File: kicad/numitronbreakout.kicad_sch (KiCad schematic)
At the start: 8 parts, among them J1 Conn_01x06, U1 HV5812WG-G, U2 IV-12, U3 IV-12, U4 LM317_TO-220

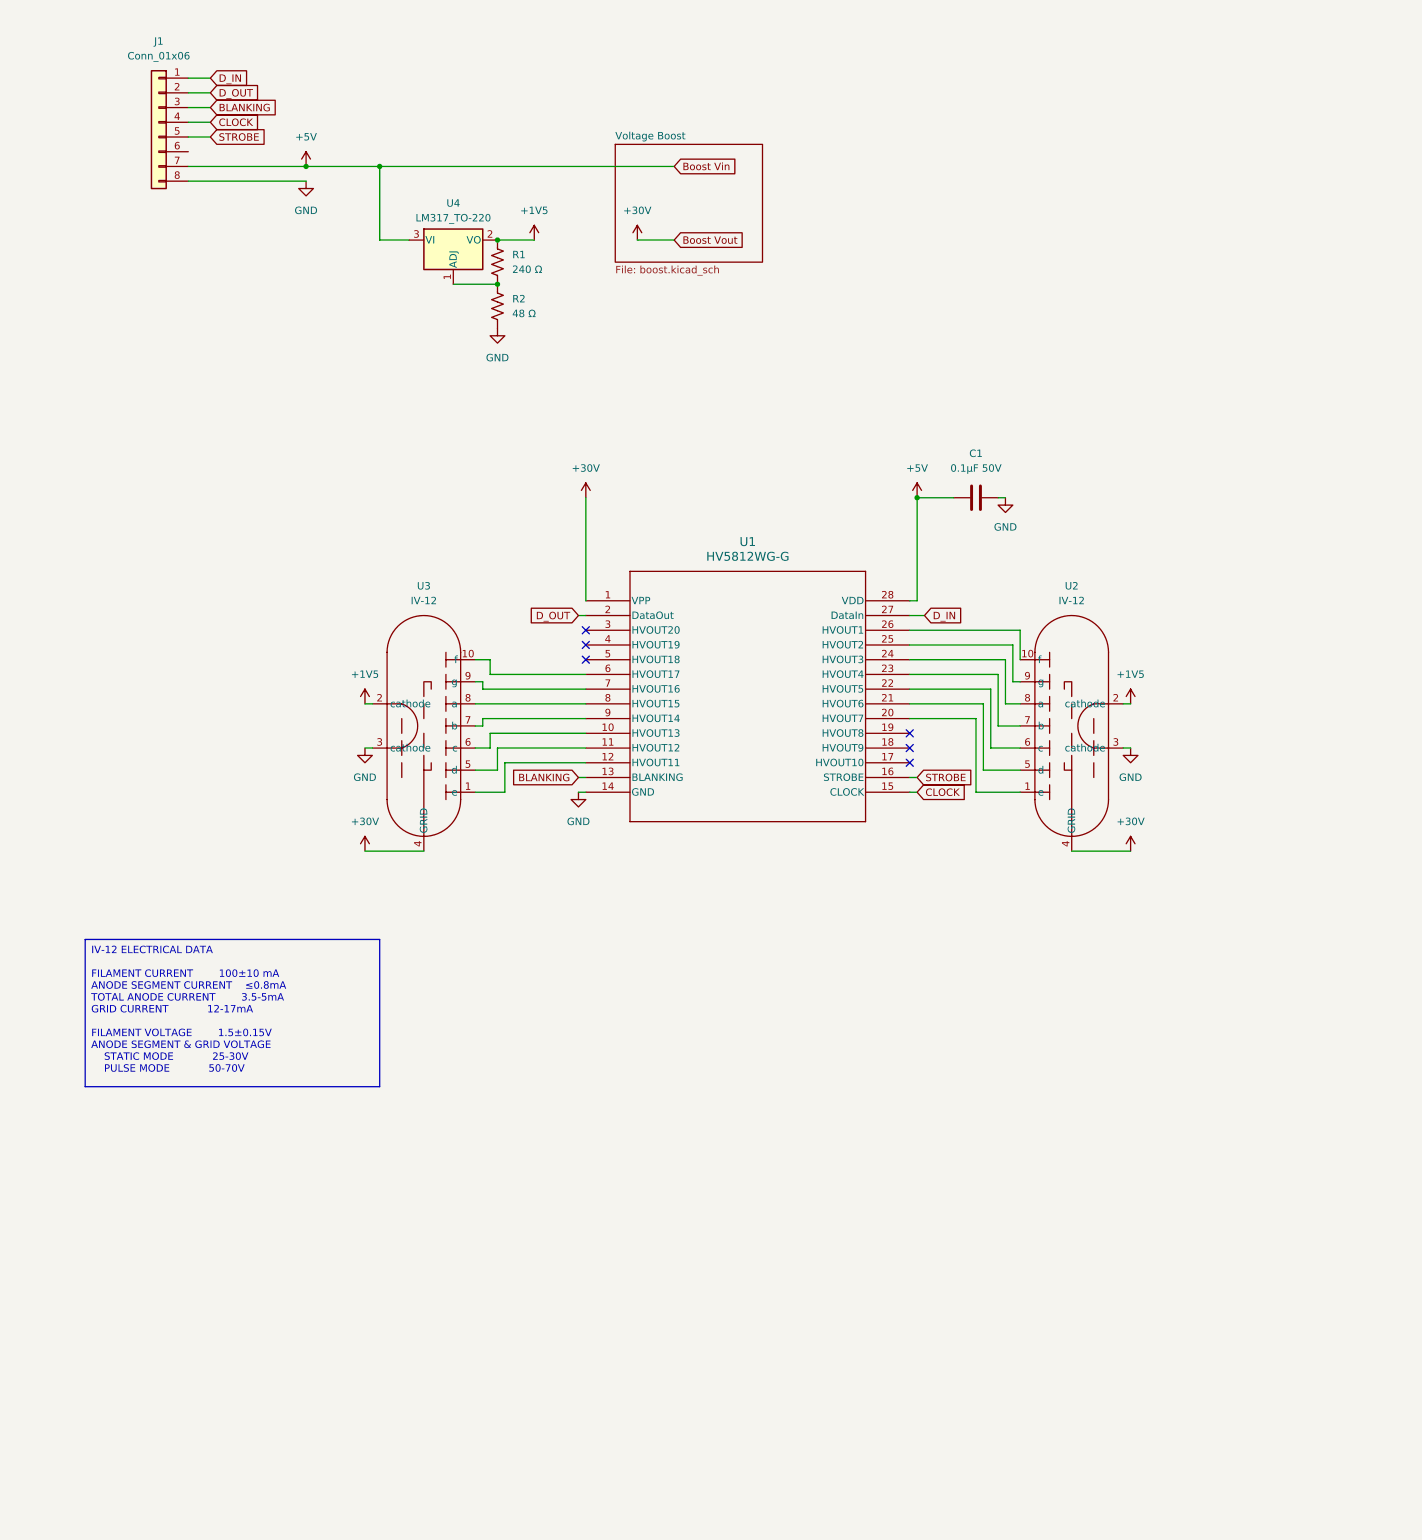
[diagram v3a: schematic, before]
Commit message: boost converter refactor
new design from web bench to reduce bom complexity & increase efficiency
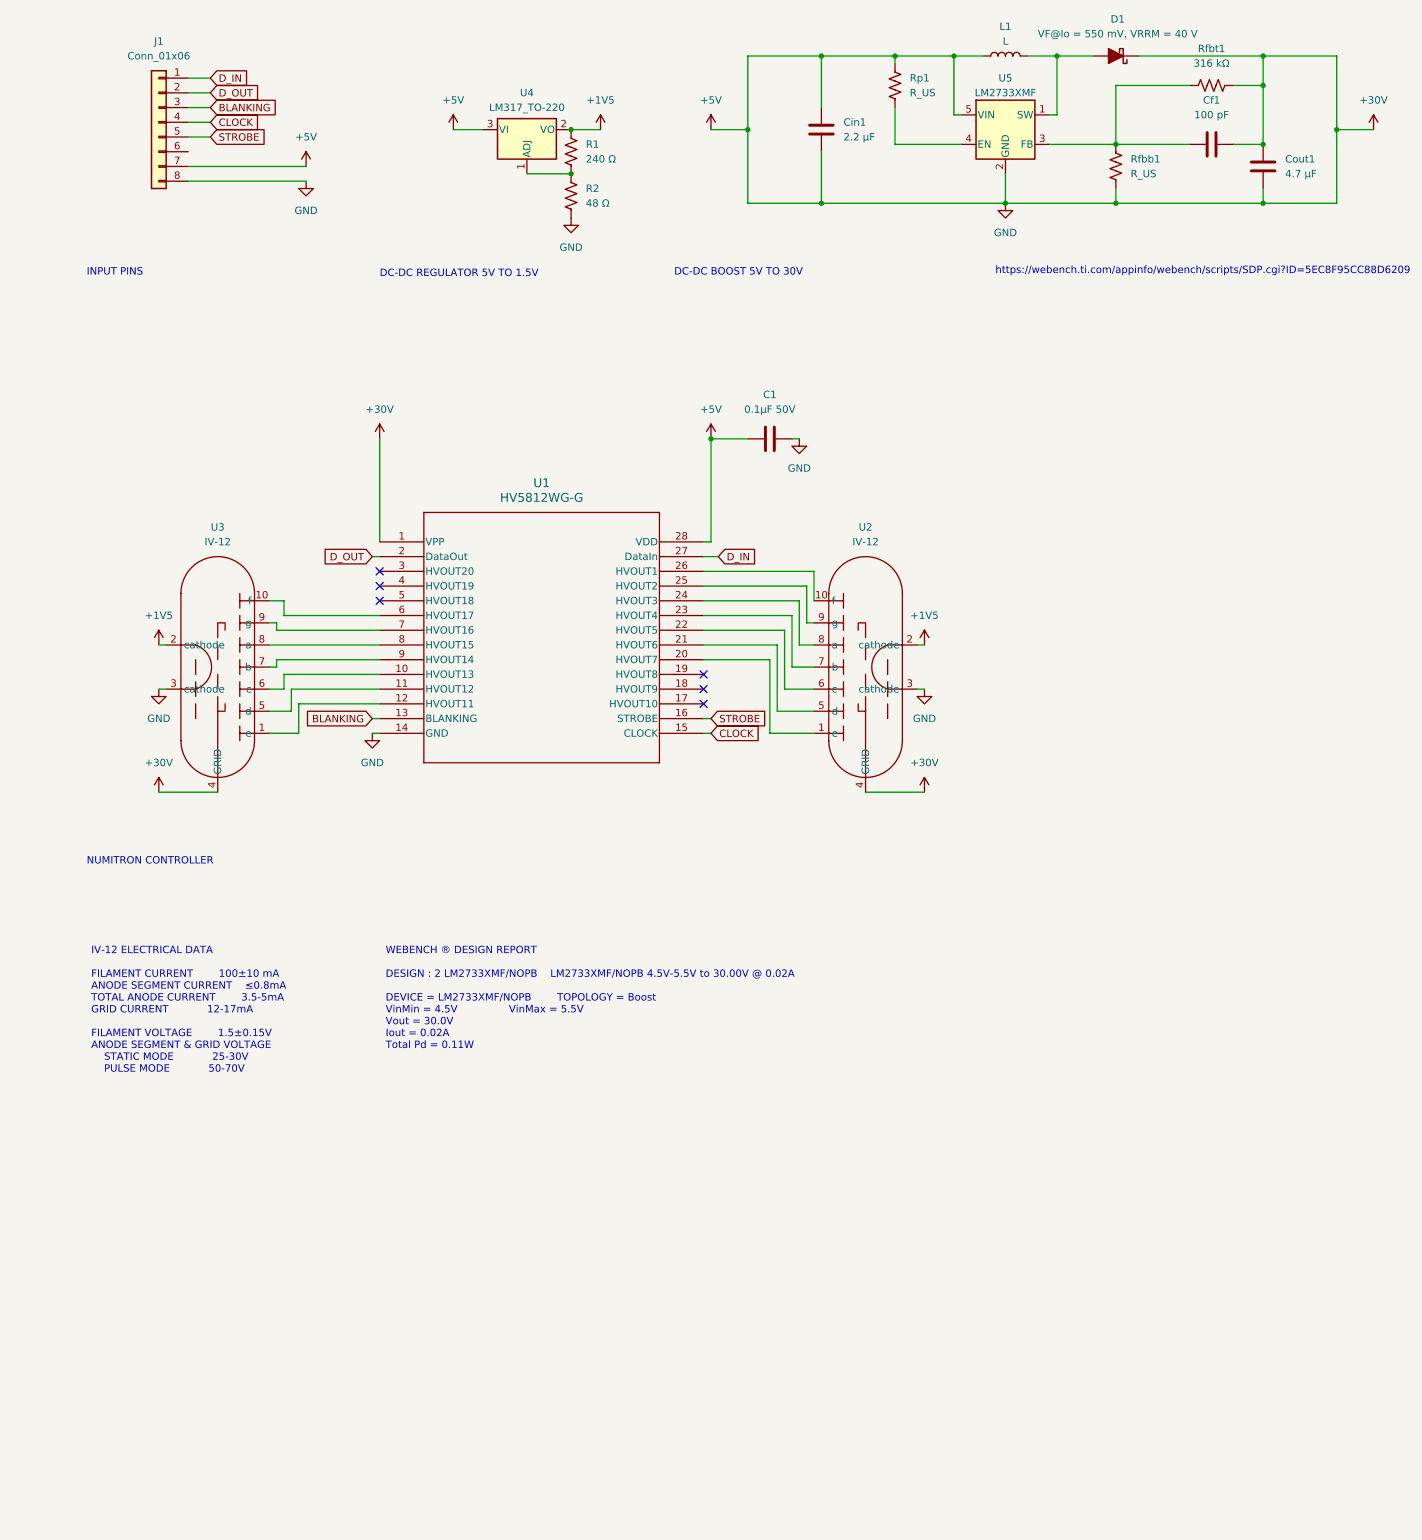
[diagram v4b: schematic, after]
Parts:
- added Cf1: 100 pF, symbol Device:C
- added Cin1: 2.2 μF, symbol Device:C
- added Cout1: 4.7 μF, symbol Device:C
- added D1: VF@Io = 550 mV, VRRM = 40 V, symbol Device:D_Schottky_Filled
- added L1: L, symbol Device:L
- added Rfbb1, Rp1: R_US, symbol Device:R_US
- added Rfbt1: 316 kΩ, symbol Device:R_US
- added U5: LM2733XMF, Package_TO_SOT_SMD:SOT-23-5, symbol Regulator_Switching:LM2733XMF
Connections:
- net +5V is gone; now on net +30V: C1.1, J1.7 (Pin_7), U1.28 (VDD), U4.3 (VI)
- net GND is gone; now on net +30V: C1.2, J1.8 (Pin_8), R2.2, U1.14 (GND), U2.3 (cathode), U3.3 (cathode)
- net +30V: now also Cf1.2, Cin1.1, Cin1.2, Cout1.1, Cout1.2, D1.1 (K), L1.1, Rfbb1.2, Rfbt1.2, Rp1.1, U5.2 (GND), U5.5 (VIN)
- new net: Rp1.2, U5.4 (EN)
- new net: D1.2 (A), L1.2, U5.1 (SW)
- new net: Cf1.1, Rfbb1.1, Rfbt1.1, U5.3 (FB)
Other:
- removed sheet Voltage Boost
- note added: "DC-DC BOOST 5V TO 30V"
- note added: "DC-DC REGULATOR 5V TO 1.5V"
- note added: "INPUT PINS"
- note added: "NUMITRON CONTROLLER"
- note added: "https://webench.ti.com/appinfo/webench/scripts/SDP.cgi?ID=5EC8F95CC88D6209"
- moved on the sheet: C1, R1, R2, U1, U2, U3, U4

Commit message: pcb layout
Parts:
- removed Cf1: 100 pF, symbol Device:C
- removed Cin1: 2.2 μF, symbol Device:C
- removed Cout1: 4.7 μF, symbol Device:C
- removed D1: VF@Io = 550 mV, VRRM = 40 V, symbol Device:D_Schottky_Filled
- removed L1: L, symbol Device:L
- removed Rfbb1, Rp1: R_US, symbol Device:R_US
- removed Rfbt1: 316 kΩ, symbol Device:R_US
- removed U5: LM2733XMF, Package_TO_SOT_SMD:SOT-23-5, symbol Regulator_Switching:LM2733XMF
- R1: footprint Resistor_SMD:R_0402_1005Metric -> Resistor_SMD:R_0402_1005Metric_Pad0.72x0.64mm_HandSolder; MFR (none) -> Vishay Dale; Part No (none) -> CRCW0402240RFKED
- R2: footprint Resistor_SMD:R_0402_1005Metric -> Resistor_SMD:R_0402_1005Metric_Pad0.72x0.64mm_HandSolder; MFR (none) -> Vishay Dale; Part No (none) -> CRCW040248R7FKED
- U2: renamed from U4; MFR (none) -> Texas Instruments; Part No (none) -> LM317TNS/NOPB-ND
- U3: renamed from U1; MFR (none) -> Microchip Technology; Part No (none) -> HV5812WG-G
- renumbered U2 to U4, U3 to U5
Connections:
- net +30V: no longer C1.1, C1.2, J1.7 (Pin_7), J1.8 (Pin_8), R2.2, U2.3 (VI), U3.14 (GND), U3.28 (VDD), U4.3 (cathode), U5.3 (cathode)
- new net +5V: C1.1, J1.7 (Pin_7), U2.3 (VI), U3.28 (VDD)
- new net GND: C1.2, J1.8 (Pin_8), R2.2, U3.14 (GND), U4.3 (cathode), U5.3 (cathode)
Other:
- added sheet DC-DC BOOST 5V TO 30V (stepup.kicad_sch)
- note removed: "DC-DC BOOST 5V TO 30V"
- note removed: "https://webench.ti.com/appinfo/webench/scripts/SDP.cgi?ID=5EC8F95CC88D6209"

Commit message: finished wiring everything but 30v
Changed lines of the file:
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@@
-	(wire
-		(pts
-			(xy 138.43 38.1) (xy 139.7 38.1)
-		)
-		(stroke
-			(width 0)
-			(type default)
-		)
-	)
 	(wire
 		(pts
@@
 		(pts
 			(xy 48.26 138.43) (xy 44.45 138.43)
-		)
-		(stroke
-			(width 0)
-			(type default)
-		)
-	)
-	(wire
-		(pts
-			(xy 138.43 50.8) (xy 139.7 50.8)
 		)
 		(stroke
@@
 	(text "INPUT PINS"
 		(exclude_from_sim no)
-		(at 12.954 63.5 0)
+		(at 12.7 63.5 0)
 		(effects
 			(font
@@
 		)
 	)
-	(global_label "BOOST_VIN"
+	(global_label "CLOCK"
 		(shape input)
-		(at 139.7 38.1 0)
+		(at 120.65 142.24 0)
 		(fields_autoplaced yes)
 		(effects
@@
 		)
 		(property "Intersheetrefs" "${INTERSHEET_REFS}"
-			(at 152.7848 38.1 0)
+			(at 129.8038 142.24 0)
 			(effects
 				(font
@@
 		)
 	)
-	(global_label "CLOCK"
+	(global_label "BLANKING"
 		(shape input)
-		(at 120.65 142.24 0)
+		(at 62.23 139.7 180)
 		(fields_autoplaced yes)
 		(effects
@@
 				(size 1.27 1.27)
 			)
-			(justify left)
+			(justify right)
 		)
 		(property "Intersheetrefs" "${INTERSHEET_REFS}"
-			(at 129.8038 142.24 0)
-			(effects
-				(font
-					(size 1.27 1.27)
-				)
-				(justify left)
-				(hide yes)
-			)
-		)
-	)
-	(global_label "BLANKING"
+			(at 50.0523 139.7 0)
+			(effects
+				(font
+					(size 1.27 1.27)
+				)
+				(justify right)
+				(hide yes)
+			)
+		)
+	)
+	(global_label "D_IN"
 		(shape input)
-		(at 62.23 139.7 180)
+		(at 121.92 111.76 0)
 		(fields_autoplaced yes)
 		(effects
@@
 				(size 1.27 1.27)
 			)
-			(justify right)
-		)
-		(property "Intersheetrefs" "${INTERSHEET_REFS}"
-			(at 50.0523 139.7 0)
-			(effects
-				(font
-					(size 1.27 1.27)
-				)
-				(justify right)
-				(hide yes)
-			)
-		)
-	)
-	(global_label "D_IN"
-		(shape input)
-		(at 121.92 111.76 0)
-		(fields_autoplaced yes)
-		(effects
-			(font
-				(size 1.27 1.27)
-			)
 			(justify left)
 		)
 		(property "Intersheetrefs" "${INTERSHEET_REFS}"
 			(at 129.0781 111.76 0)
-			(effects
-				(font
-					(size 1.27 1.27)
-				)
-				(justify left)
-				(hide yes)
-			)
-		)
-	)
-	(global_label "BOOST_VOUT"
-		(shape input)
-		(at 139.7 50.8 0)
-		(fields_autoplaced yes)
-		(effects
-			(font
-				(size 1.27 1.27)
-			)
-			(justify left)
-		)
-		(property "Intersheetrefs" "${INTERSHEET_REFS}"
-			(at 154.4781 50.8 0)
 			(effects
 				(font
@@
 	)
 	(symbol
-		(lib_id "power:+5V")
-		(at 138.43 38.1 0)
-		(unit 1)
-		(exclude_from_sim no)
-		(in_bom yes)
-		(on_board yes)
-		(dnp no)
-		(fields_autoplaced yes)
-		(property "Reference" "#PWR015"
-			(at 138.43 41.91 0)
-			(effects
-				(font
-					(size 1.27 1.27)
-				)
-				(hide yes)
-			)
-		)
-		(property "Value" "+5V"
-			(at 138.43 33.02 0)
-			(effects
-				(font
-					(size 1.27 1.27)
-				)
-			)
-		)
-		(property "Footprint" ""
-			(at 138.43 38.1 0)
-			(effects
-				(font
-					(size 1.27 1.27)
-				)
-				(hide yes)
-			)
-		)
-		(property "Datasheet" ""
-			(at 138.43 38.1 0)
-			(effects
-				(font
-					(size 1.27 1.27)
-				)
-				(hide yes)
-			)
-		)
-		(property "Description" "Power symbol creates a global label with name \"+5V\""
-			(at 138.43 38.1 0)
-			(effects
-				(font
-					(size 1.27 1.27)
-				)
-				(hide yes)
-			)
-		)
-		(pin "1"
-		)
-		(instances
-			(project "numitronbreakout"
-				(path "/361dfde8-db82-4f79-b593-288fe0fd1919"
-					(reference "#PWR015")
-					(unit 1)
-				)
-			)
-		)
-	)
-	(symbol
 		(lib_id "power:+1V5")
 		(at 25.4 127 0)
@@
 					(unit 1)
 				)
-			)
-		)
-	)
-	(symbol
-		(lib_id "power:+36V")
-		(at 138.43 50.8 0)
-		(unit 1)
-		(exclude_from_sim no)
-		(in_bom yes)
-		(on_board yes)
-		(dnp no)
-		(fields_autoplaced yes)
-		(property "Reference" "#PWR018"
-			(at 138.43 54.61 0)
-			(effects
-				(font
-					(size 1.27 1.27)
-				)
-				(hide yes)
-			)
-		)
-		(property "Value" "+30V"
-			(at 138.43 45.72 0)
-			(effects
-				(font
-					(size 1.27 1.27)
-				)
-			)
-		)
-		(property "Footprint" ""
-			(at 138.43 50.8 0)
-			(effects
-				(font
-					(size 1.27 1.27)
-				)
-				(hide yes)
-			)
-		)
-		(property "Datasheet" ""
-			(at 138.43 50.8 0)
-			(effects
-				(font
-					(size 1.27 1.27)
-				)
-				(hide yes)
-			)
-		)
-		(property "Description" "Power symbol creates a global label with name \"+36V\""
-			(at 138.43 50.8 0)
-			(effects
-				(font
-					(size 1.27 1.27)
-				)
-				(hide yes)
-			)
-		)
-		(pin "1"
-		)
-		(instances
-			(project "numitronbreakout"
-				(path "/361dfde8-db82-4f79-b593-288fe0fd1919"
-					(reference "#PWR018")
-					(unit 1)
-				)

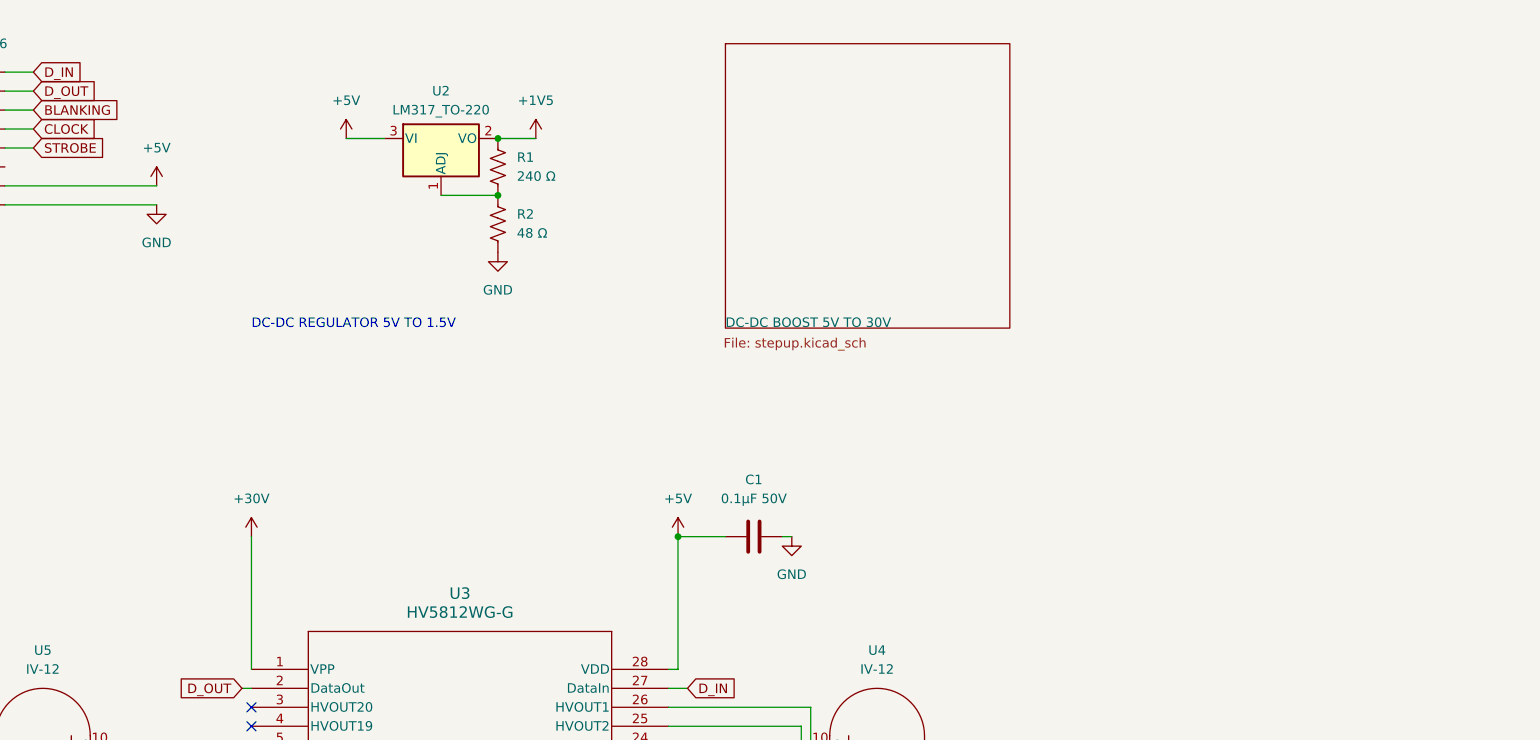
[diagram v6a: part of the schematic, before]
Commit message: finally decided v boost solution, finished pathing pcb
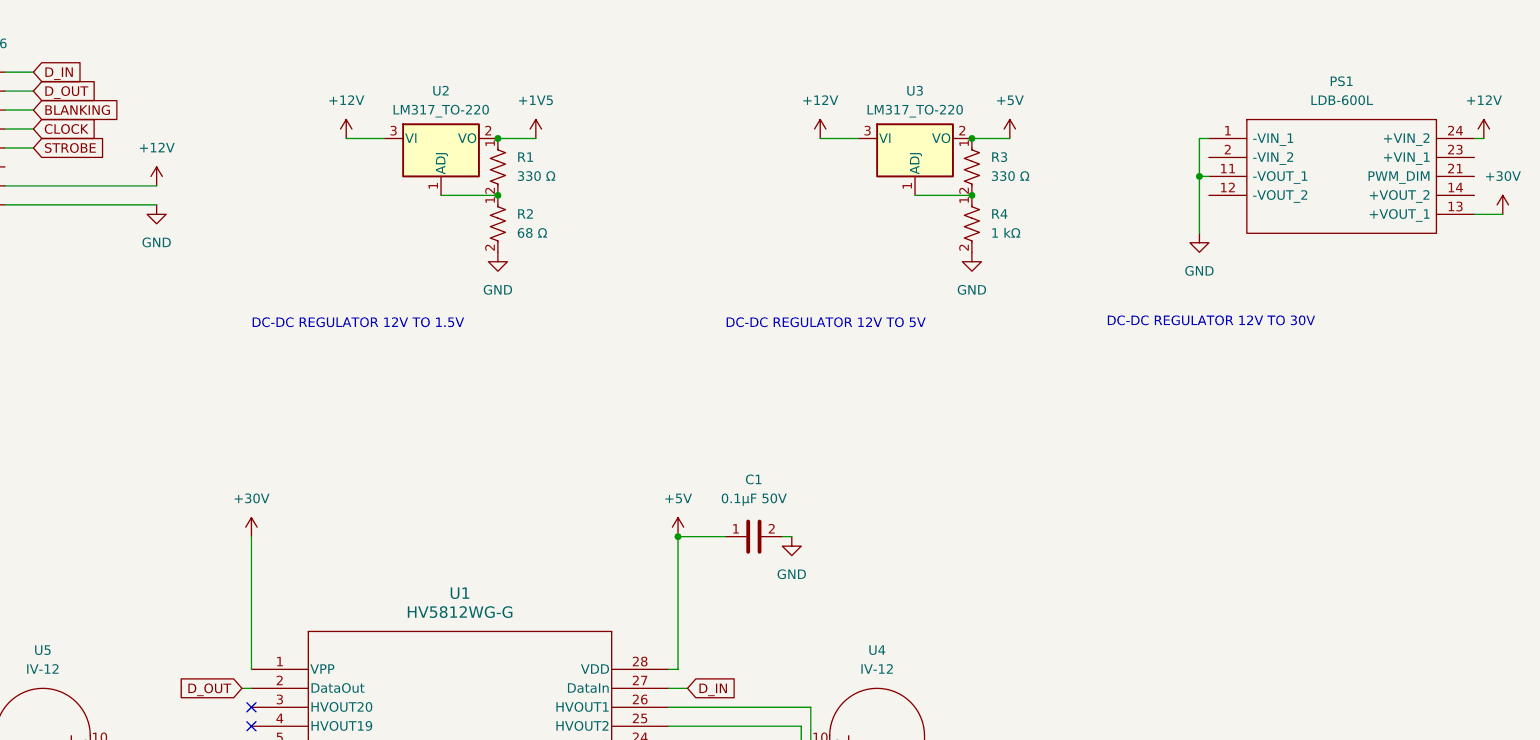
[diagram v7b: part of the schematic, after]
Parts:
- added PS1: LDB-600L, NewFootprints:LDB600L, symbol NewSymbols:LDB-600L
- added R3: 330 Ω, Resistor_SMD:R_0402_1005Metric_Pad0.72x0.64mm_HandSolder, symbol Device:R_US
- added R4: 1 kΩ, Resistor_SMD:R_0402_1005Metric_Pad0.72x0.64mm_HandSolder, symbol Device:R_US
- added U3: LM317_TO-220, Package_TO_SOT_THT:TO-220-3_Vertical, symbol Regulator_Linear:LM317_TO-220
- R1: value 240 Ω -> 330 Ω
- R2: value 48 Ω -> 68 Ω
- renumbered U3 to U1
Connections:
- net +30V: now also PS1.13 (+VOUT_1)
- net +5V: now also R3.1, U3.2 (VO); no longer J1.7 (Pin_7), U2.3 (VI)
- net GND: now also PS1.1 (-VIN_1), PS1.11 (-VOUT_1), R4.2
- new net: R3.2, R4.1, U3.1 (ADJ)
- new net +12V: J1.7 (Pin_7), PS1.24 (+VIN_2), U2.3 (VI), U3.3 (VI)
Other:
- removed sheet DC-DC BOOST 5V TO 30V
- note added: "DC-DC REGULATOR 12V TO 1.5V"
- note added: "DC-DC REGULATOR 12V TO 30V"
- note added: "DC-DC REGULATOR 12V TO 5V"
- note removed: "DC-DC REGULATOR 5V TO 1.5V"
